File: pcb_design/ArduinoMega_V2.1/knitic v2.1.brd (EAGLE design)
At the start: 129.8 x 75.6 mm, 23 parts

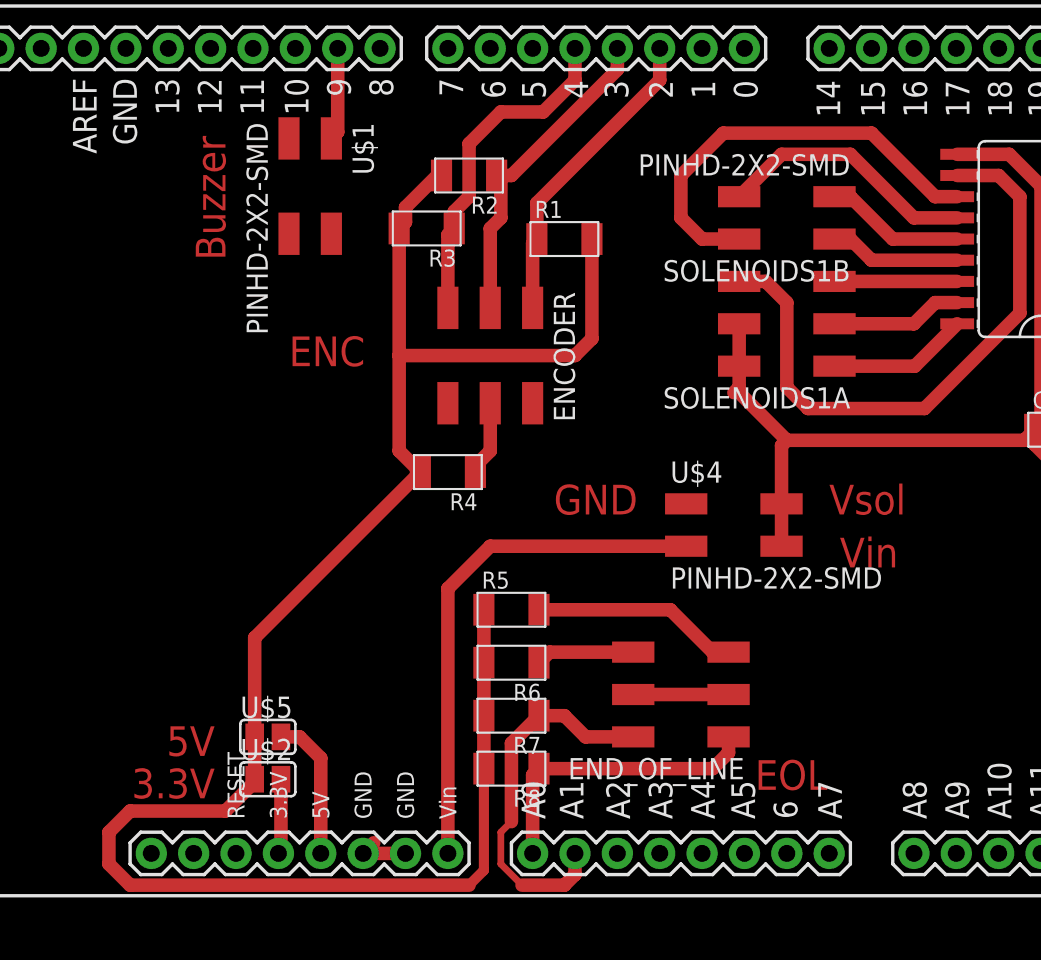
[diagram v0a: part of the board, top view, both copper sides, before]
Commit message: Add info and reset/led on pcb design
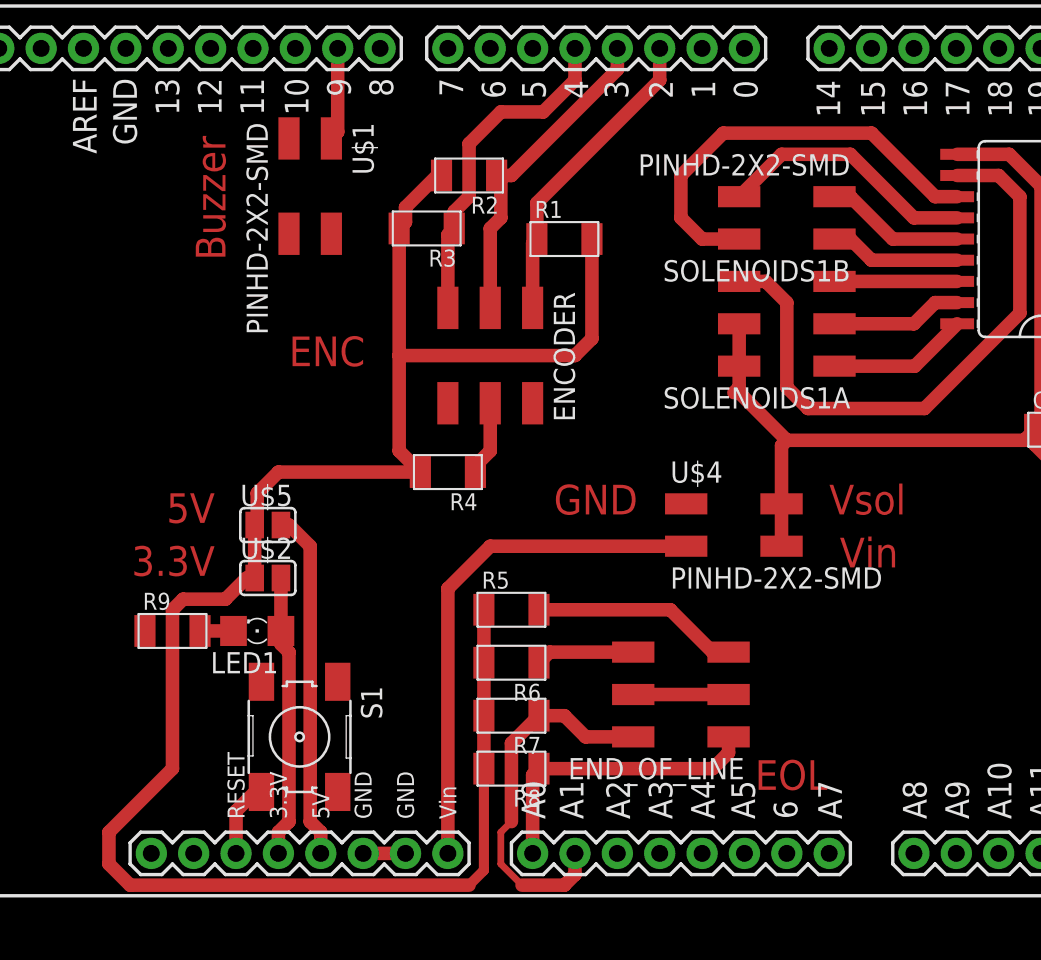
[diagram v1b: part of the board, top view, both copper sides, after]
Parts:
- added LED1: (no value), adafruit:1206
- added R9: 499, fab:R1206FAB
- added S1: (no value), fab:6MM_SWITCH
- moved U$5 12.7 mm to (21.0, 26.0)
- moved U$2 12.1 mm to (21.0, 22.9)
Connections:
- new net N$3: PCB1.RESET, S1.4
- new net N$6: LED1.C, R9.2
- net 3.3: now also LED1.A
- net GND: now also R9.1, S1.2
- net SO10: now also IC2.7, PCB1.35; no longer IC2.2, PCB1.25
- net SO11: now also IC2.6, PCB1.33; no longer IC2.3, PCB1.27
- net SO12: now also IC2.5, PCB1.31; no longer IC2.4, PCB1.29
- net SO13: now also IC2.4, PCB1.29; no longer IC2.5, PCB1.31
- net SO14: now also IC2.3, PCB1.27; no longer IC2.6, PCB1.33
- net SO15: now also IC2.2, PCB1.25; no longer IC2.7, PCB1.35
- net SO16: now also IC2.1, PCB1.23; no longer IC2.8, PCB1.37
- net SO9: now also IC2.8, PCB1.37; no longer IC2.1, PCB1.23
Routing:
- net SO9: track 31.9 -> 9.99 mm
- net SO16: track 9.99 -> 31.9 mm
- net SO15: track 12.0 -> 28.8 mm
- net SO10: track 28.8 -> 12.0 mm
- net 3.3: track 4.51 -> 17.0 mm
- net N$23: track 8.63 -> 21.0 mm
- net SO14: track 15.1 -> 25.0 mm
- net SO11: track 25.0 -> 15.1 mm
- net N$3: track 0.00 -> 4.54 mm
- net SO13: track 18.1 -> 21.9 mm
- net SO12: track 21.9 -> 18.1 mm
- net VCC: track 111.0 -> 114.4 mm
- net N$6: track 0.00 -> 2.01 mm
- net GND: track 87.5 -> 86.6 mm
